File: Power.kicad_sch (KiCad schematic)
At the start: 13 parts, among them J1 Amphenol ICC 10118193-0001LF, U1 LM2940LD-5.0/NOPB, U12 LM1117LD-3.3/NOPB

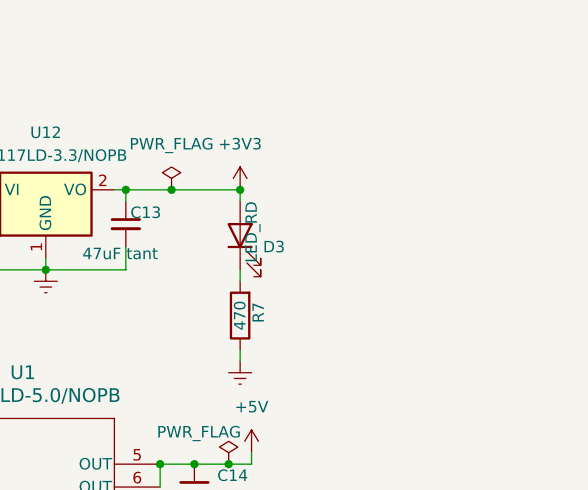
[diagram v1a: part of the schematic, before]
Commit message: Added previously missing V_CORE 1.35V regulator
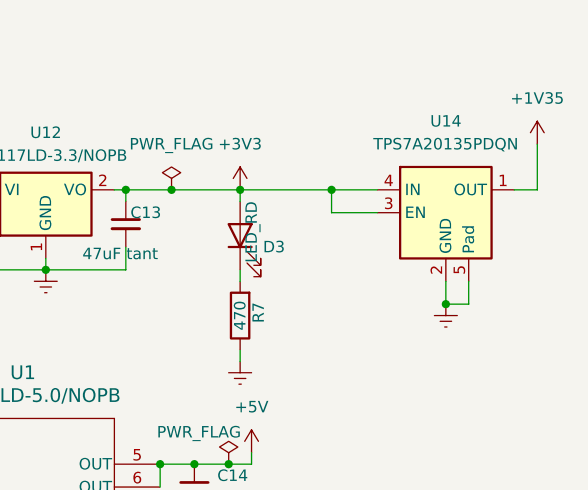
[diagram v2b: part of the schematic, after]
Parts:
- added U14: TPS7A20135PDQN, Package_DFN_QFN:DFN-6-1EP_1.2x1.2mm_P0.4mm_EP0.3x0.94mm_PullBack, symbol Regulator_Linear:TPS7A20xxxDQN
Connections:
- net +3V3: now also U14.3 (EN), U14.4 (IN)
- net GNDREF: now also U14.2 (GND), U14.5 (Pad)
- new net +1V35: U14.1 (OUT)

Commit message: Some layout tweaks
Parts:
- removed U14: TPS7A20135PDQN, Package_DFN_QFN:DFN-6-1EP_1.2x1.2mm_P0.4mm_EP0.3x0.94mm_PullBack, symbol Regulator_Linear:TPS7A20xxxDQN
- added U15: TPS7A20xxxDQN, Package_SON:Texas_X2SON-4_1x1mm_P0.65mm, symbol Regulator_Linear:TPS7A20xxxDQN
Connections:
- net +1V35: now also U15.1 (OUT)
- net +3V3: now also U15.3 (EN), U15.4 (IN)
- net GNDREF: now also U15.2 (GND), U15.5 (Pad)
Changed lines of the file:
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@@
+	)
+	(symbol
+		(lib_id "Regulator_Linear:TPS7A20xxxDQN")
+		(at 205.74 87.63 0)
+		(unit 1)
+		(exclude_from_sim no)
+		(in_bom yes)
+		(on_board yes)
+		(dnp no)
+		(fields_autoplaced yes)
+		(property "Reference" "U15"
+			(at 205.74 77.47 0)
+			(effects
+				(font
+					(size 1.27 1.27)
+				)
+			)
+		)
+		(property "Value" "TPS7A20xxxDQN"
+			(at 205.74 80.01 0)
+			(effects
+				(font
+					(size 1.27 1.27)
+				)
+			)
+		)
+		(property "Footprint" "Package_SON:Texas_X2SON-4_1x1mm_P0.65mm"
+			(at 205.74 78.74 0)
+			(effects
+				(font
+					(size 1.27 1.27)
+				)
+				(hide yes)
+			)
+		)
+		(property "Datasheet" "https://www.ti.com/lit/ds/symlink/tps7a20.pdf"
+			(at 205.74 74.93 0)
+			(effects
+				(font
+					(size 1.27 1.27)
+				)
+				(hide yes)
+			)
+		)
+		(property "Description" "300 mA Low Dropout Voltage Regulator, Fixed Output, 1.6..6.0Vin, Low-Noise (7μV RMS), 6.5μA IQ LDO, X2SON-5"
+			(at 205.74 87.63 0)
+			(effects
+				(font
+					(size 1.27 1.27)
+				)
+				(hide yes)
+			)
+		)
+		(pin "4"
+		)
+		(pin "2"
+		)
+		(pin "3"
+		)
+		(pin "1"
+		)
+		(pin "5"
+		)
+		(instances
+			(project ""
+				(path "/b8dcf6c3-e00e-4510-86f1-1869a84939df/291ae41e-8f75-444f-8dd6-d72f3862478e"
+					(reference "U15")
+					(unit 1)
+				)
+			)
+		)
 	)
 	(symbol
@@
 					(unit 1)
 				)
-			)
-		)
-	)
-	(symbol
-		(lib_id "Regulator_Linear:TPS7A20xxxDQN")
-		(at 205.74 87.63 0)
-		(unit 1)
-		(exclude_from_sim no)
-		(in_bom yes)
-		(on_board yes)
-		(dnp no)
-		(fields_autoplaced yes)
-		(property "Reference" "U14"
-			(at 205.74 77.47 0)
-			(effects
-				(font
-					(size 1.27 1.27)
-				)
-			)
-		)
-		(property "Value" "TPS7A20135PDQN"
-			(at 205.74 80.01 0)
-			(effects
-				(font
-					(size 1.27 1.27)
-				)
-			)
-		)
-		(property "Footprint" "Package_DFN_QFN:DFN-6-1EP_1.2x1.2mm_P0.4mm_EP0.3x0.94mm_PullBack"
-			(at 205.74 78.74 0)
-			(effects
-				(font
-					(size 1.27 1.27)
-				)
-				(hide yes)
-			)
-		)
-		(property "Datasheet" "https://www.ti.com/lit/ds/symlink/tps7a20.pdf"
-			(at 205.74 74.93 0)
-			(effects
-				(font
-					(size 1.27 1.27)
-				)
-				(hide yes)
-			)
-		)
-		(property "Description" "300 mA Low Dropout Voltage Regulator, Fixed Output, 1.6..6.0Vin, Low-Noise (7μV RMS), 6.5μA IQ LDO, X2SON-5"
-			(at 205.74 87.63 0)
-			(effects
-				(font
-					(size 1.27 1.27)
-				)
-				(hide yes)
-			)
-		)
-		(pin "4"
-		)
-		(pin "2"
-		)
-		(pin "3"
-		)
-		(pin "5"
-		)
-		(pin "1"
-		)
-		(instances
-			(project ""
-				(path "/b8dcf6c3-e00e-4510-86f1-1869a84939df/291ae41e-8f75-444f-8dd6-d72f3862478e"
-					(reference "U14")
-					(unit 1)
-				)

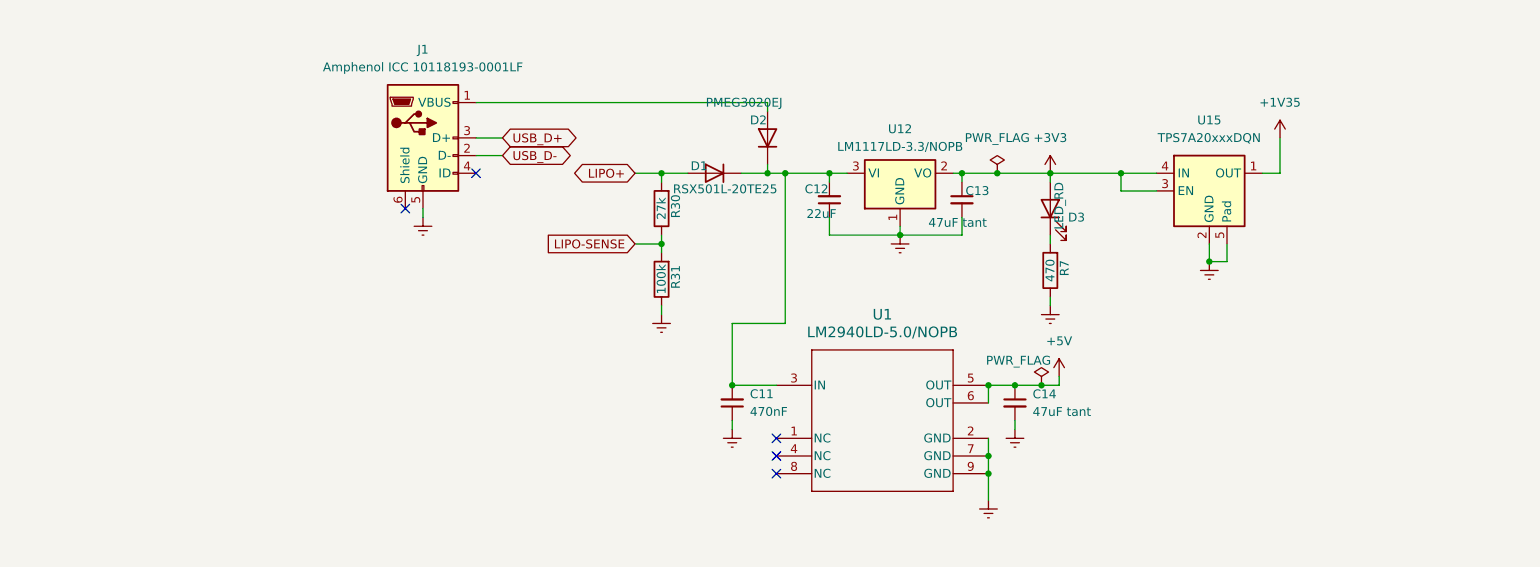
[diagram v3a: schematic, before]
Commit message: Started new layout and updated power circuitry
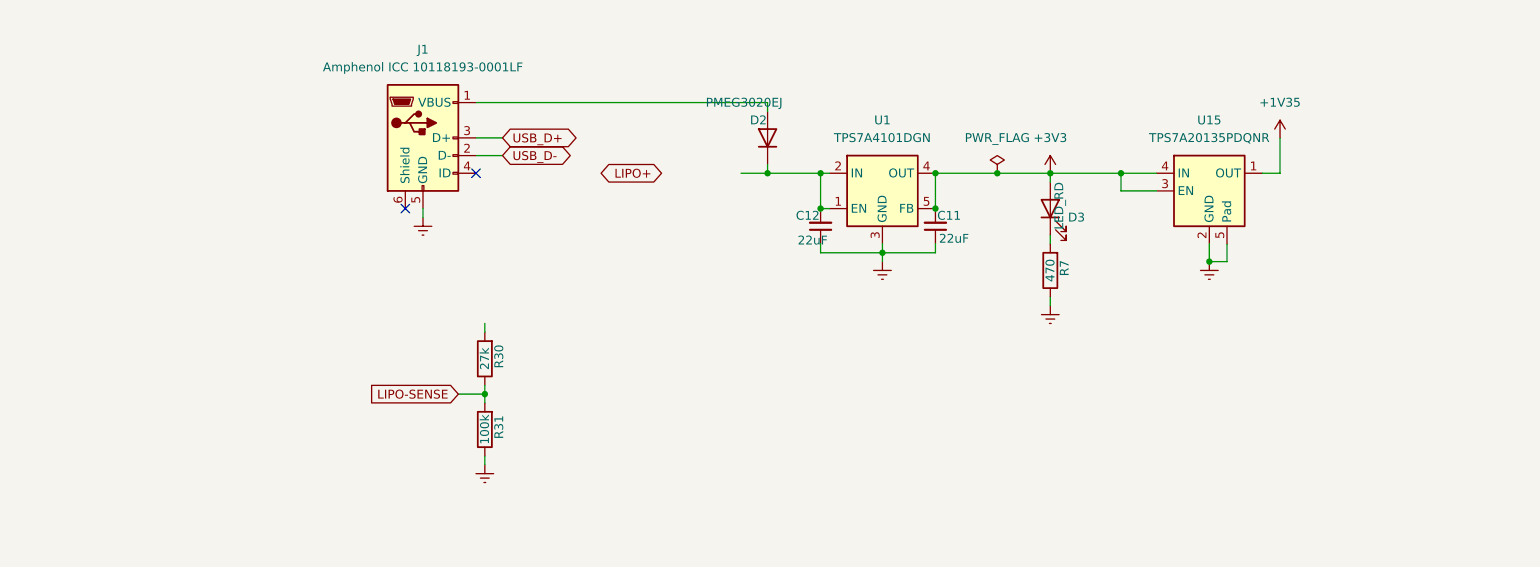
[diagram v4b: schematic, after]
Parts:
- removed C13, C14: 47uF tant, Capacitor_Tantalum_SMD:CP_EIA-2012-15_AVX-P, symbol Device:C_Small
- removed D1: RSX501L-20TE25, Diode_SMD:D_SMA, symbol Device:D
- removed U1: LM2940LD-5.0/NOPB, WINTERfootprints:NGN0008A, symbol WINTER_components:LM2940LD-5.0_NOPB
- removed U12: LM1117LD-3.3/NOPB, Package_TO_SOT_SMD:TO-252-3_TabPin2, symbol Regulator_Linear:LM1117DT-3.3
- added U1: TPS7A4101DGN, Package_TO_SOT_SMD:SOT-223-6, symbol Regulator_Linear:TPS7A4101DGN
- C11: value 470nF -> 22uF; Product ID CL10B474KA8NFNC -> GRM188C61E226ME01W
- U15: value TPS7A20xxxDQN -> TPS7A20135PDQNR
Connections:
- net +3V3: now also C11.2, U1.4 (OUT), U1.5 (FB)
- net GNDREF: now also U1.3 (GND), U1.6 (GND)
- net LIPO+: no longer R30.2
- net at C12.2, D2.1 (K): now also U1.1 (EN), U1.2 (IN); no longer C11.2
- no-connect marks 5 -> 2
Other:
- moved on the sheet: C12, R30, R31

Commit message: updated power delivery and component choices. v4 now ready
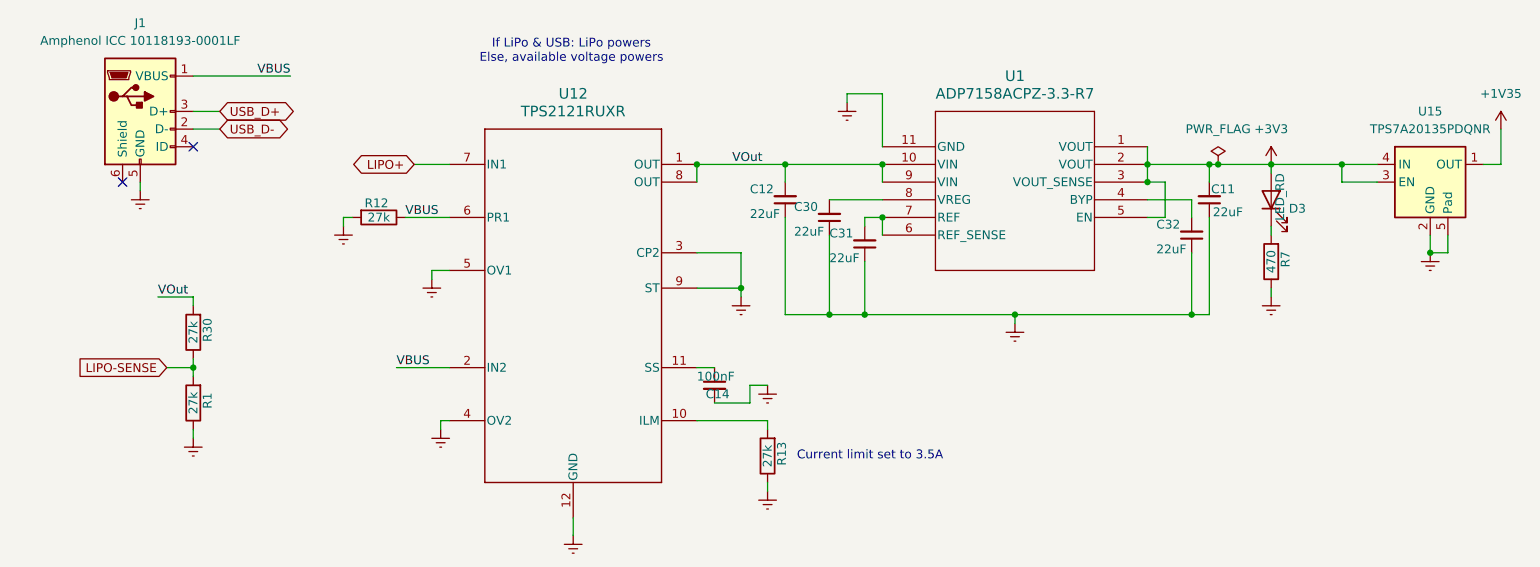
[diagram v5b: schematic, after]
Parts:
- removed D2: PMEG3020EJ, Diode_SMD:D_SOD-323F, symbol Device:D
- removed R31: 100k, Resistor_SMD:R_0603_1608Metric, symbol Device:R
- removed U1: TPS7A4101DGN, Package_TO_SOT_SMD:SOT-223-6, symbol Regulator_Linear:TPS7A4101DGN
- added C14: 100nF, Capacitor_SMD:C_0603_1608Metric, symbol Device:C_Small
- added C30, C31, C32: 22uF, Capacitor_SMD:C_0603_1608Metric, symbol Device:C_Small
- added R1, R12, R13: 27k, Resistor_SMD:R_0603_1608Metric, symbol Device:R
- added U1: ADP7158ACPZ-3.3-R7, WINTERfootprints:CP-10-9_ADI, symbol WINTER_components:ADP7158ACPZ-3.3-R7
- added U12: TPS2121RUXR, WINTERfootprints:RUX0012A, symbol WINTER_components:TPS2121RUXR
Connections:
- net +3V3: now also U1.1 (VOUT), U1.2 (VOUT), U1.3 (VOUT_SENSE), U1.5 (EN)
- net GNDREF: now also C14.2, C30.1, C31.1, C32.1, R1.1, R12.2, R13.1, U1.11 (GND), U12.12 (GND), U12.3 (CP2), U12.4 (OV2), U12.5 (OV1), U12.9 (ST)
- net LIPO+: now also U12.7 (IN1)
- net LIPO-SENSE: now also R1.2
- net VBUS: now reaches J1.1 (VBUS)
- net VBUS: now also R12.1, U12.2 (IN2), U12.6 (PR1)
- net VOut: now reaches C12.2
- net VOut: now also R30.2, U1.10 (VIN), U1.9 (VIN), U12.1 (OUT), U12.8 (OUT)
- new net: C14.1, U12.11 (SS)
- new net: C30.2, U1.8 (VREG)
- new net: R13.2, U12.10 (ILM)
- new net: C32.2, U1.4 (BYP)
- new net: C31.2, U1.6 (REF_SENSE), U1.7 (REF)
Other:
- note added: "Current limit set to 3.5A"
- note added: "If LiPo & USB: LiPo powers Else, available voltage powers"
- moved on the sheet: C11, C12, D3, J1, R30, R7, U15

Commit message: Fixed power distribution and made small improvements. Updated revision number
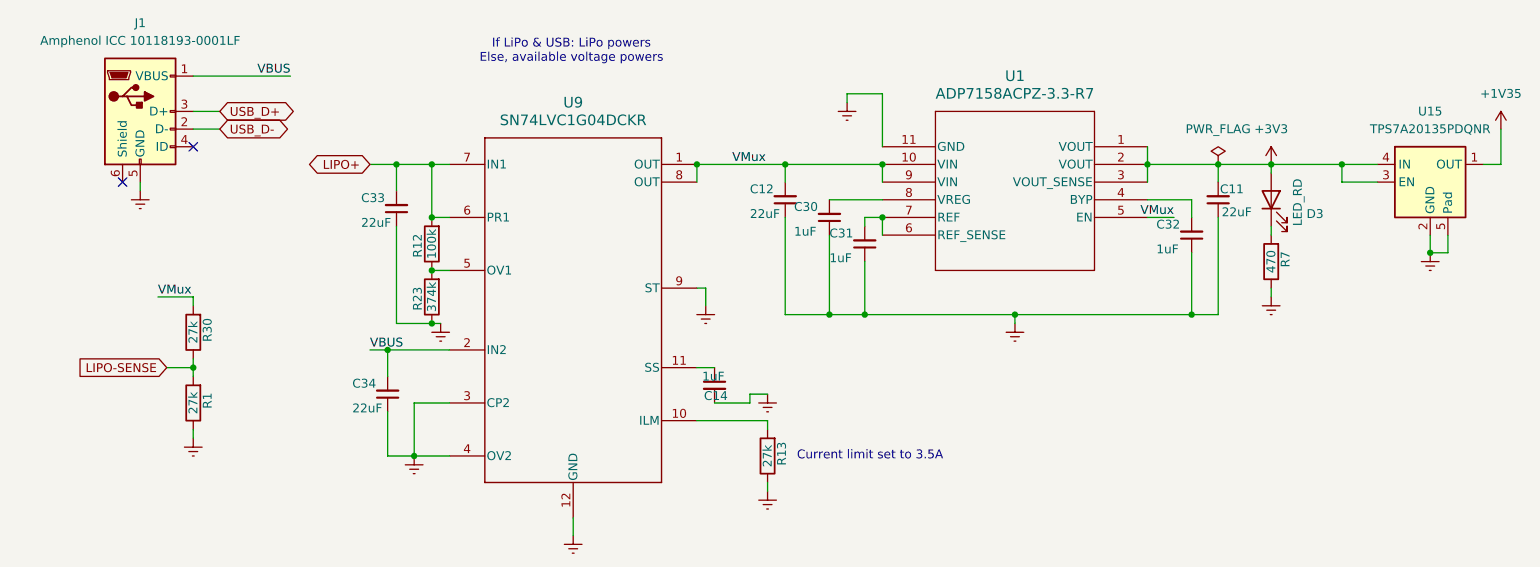
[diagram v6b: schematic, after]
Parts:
- removed U12: TPS2121RUXR, WINTERfootprints:RUX0012A, symbol WINTER_components:TPS2121RUXR
- added C33, C34: 22uF, Capacitor_SMD:C_0603_1608Metric, symbol Device:C_Small
- added R23: 374k, Resistor_SMD:R_0603_1608Metric, symbol Device:R
- added U9: SN74LVC1G04DCKR, WINTERfootprints:RUX0012A, symbol WINTER_components:TPS2121RUXR
- C14: value 100nF -> 1uF; Product ID CL10B104KB8NNNL -> CL10B105KP8NNNC
- C30, C31, C32: value 22uF -> 1uF; Product ID GRM188C61E226ME01W -> CL10B105KP8NNNC
- R12: value 27k -> 100k; LCSC C22967 -> C23162; Product ID RMCF0603JT27K0 -> ERJ-PA3J472V
- U1: Product ID (none) -> ADP7158ACPZ-3.3-R7
- U15: Product ID (none) -> TPS7A20135PDQNR
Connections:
- net +3V3: no longer U1.5 (EN)
- net GNDREF: now also C33.1, C34.1, R23.1, U9.12 (GND), U9.3 (CP2), U9.4 (OV2), U9.9 (ST); no longer R12.2
- net LIPO+: now also R12.2, C33.2, U9.6 (PR1), U9.7 (IN1)
- net VBUS: now also C34.2, U9.2 (IN2); no longer R12.1
- net at C14.1: now also U9.11 (SS)
- net at R13.2: now also U9.10 (ILM)
- net VOut renamed VMux
- net VMux: now also U1.5 (EN), U9.1 (OUT), U9.8 (OUT)
- new net: R12.1, R23.2, U9.5 (OV1)
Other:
- moved on the sheet: C11
